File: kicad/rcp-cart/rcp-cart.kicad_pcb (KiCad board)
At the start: 2 copper layers, 2 parts

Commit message: WIP
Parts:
- CONN_EXP2: moved to B.Cu
- moved CONN_EXP2 11.8 mm to (207.3, 111.4), turned to 180 degrees

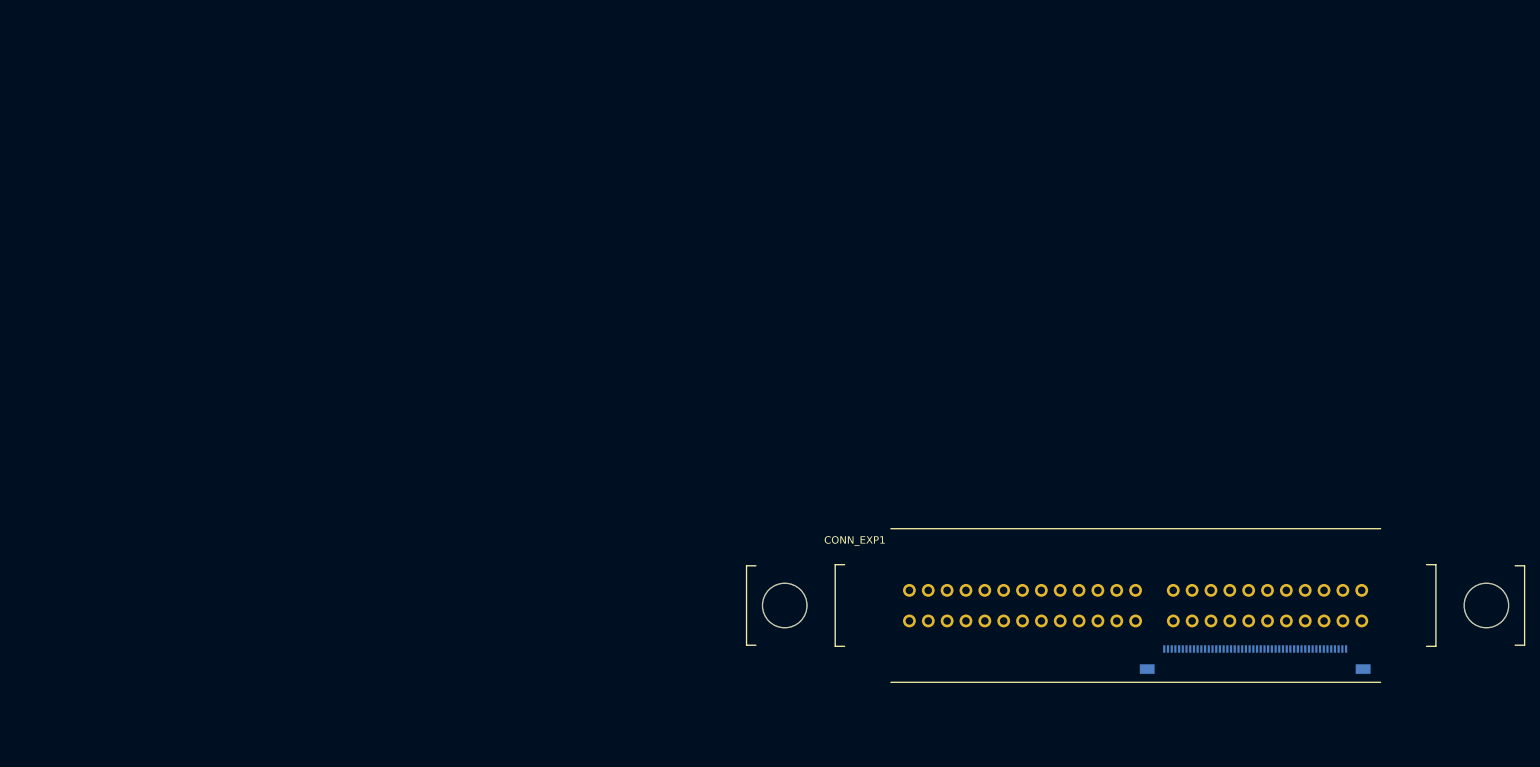
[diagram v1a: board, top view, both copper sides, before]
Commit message: Routing in progress, almost completed
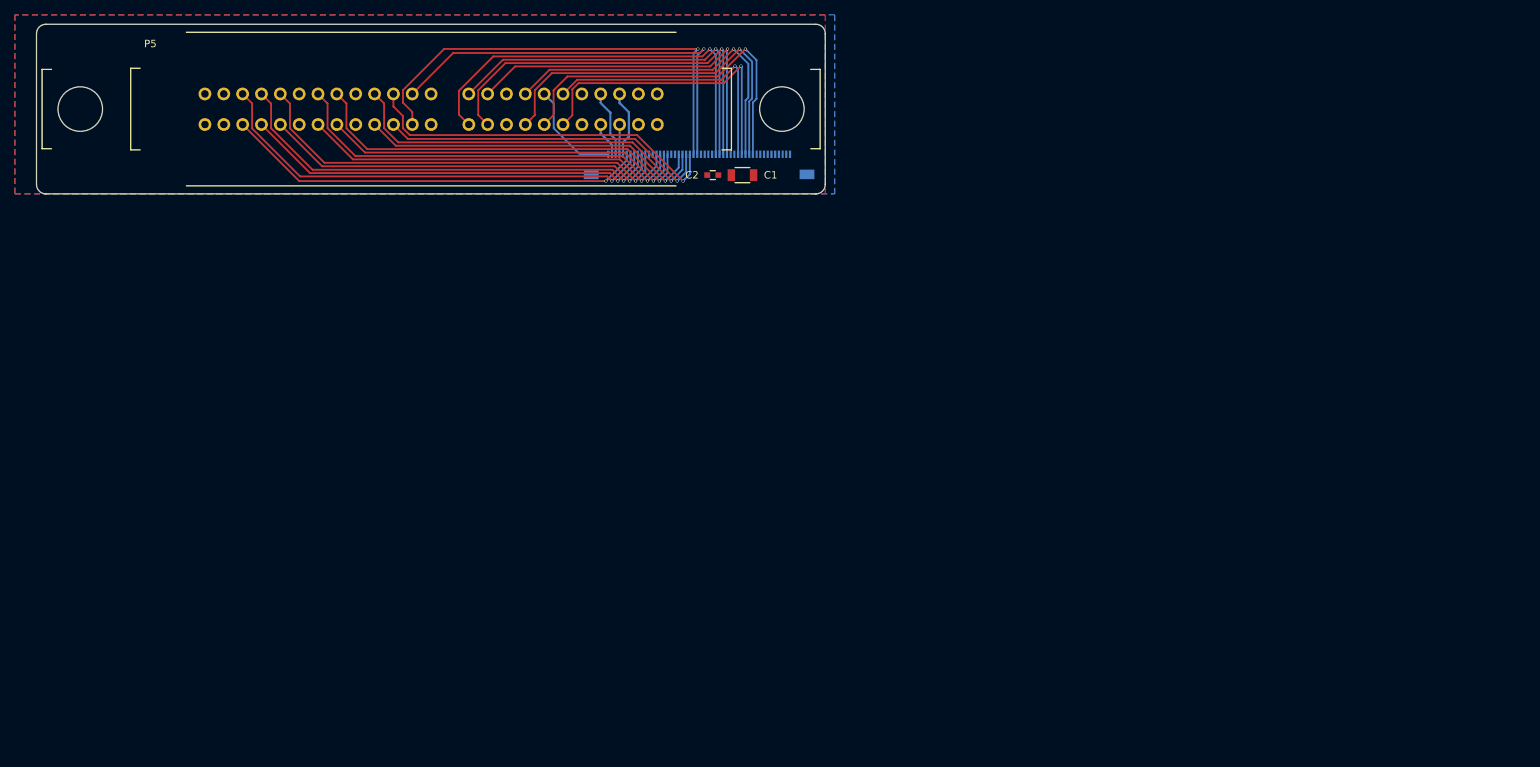
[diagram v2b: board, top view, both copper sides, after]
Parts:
- removed CONN_EXP1: CART-EDGE, n64:cart-edge-2x25-2.54mm
- removed CONN_EXP2: CART-EDGE, n64:connector-molex-502790-5091
- added C1: 4.7uF, n64:C_1206, F.Cu at (126.0, 47.0)
- added C2: .1uF, n64:C_0603, F.Cu at (122.0, 47.0)
- added P5: CART-EDGE, n64:cart-edge-2x25-2.54mm, F.Cu at (53.6, 38.1)
- added TO MAIN BOARD: 502790-5091, n64:connector-molex-502790-5091, B.Cu at (132.4, 44.7)
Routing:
- net /CART_ADDR10: track 0.00 -> 61.6 mm, vias 0 -> 1
- net /CART_ADDR00: track 0.00 -> 61.2 mm, vias 0 -> 1
- net /CART_ADDR01: track 0.00 -> 60.0 mm, vias 0 -> 1
- net /CART_ADDR02: track 0.00 -> 58.8 mm, vias 0 -> 1
- net /CART_ADDR15: track 0.00 -> 56.9 mm, vias 0 -> 1
- net /CART_ADDR05: track 0.00 -> 56.4 mm, vias 0 -> 1
- net /CART_ADDR09: track 0.00 -> 55.8 mm, vias 0 -> 1
- net /CART_ADDR14: track 0.00 -> 55.7 mm, vias 0 -> 1
- net /CART_ADDR03: track 0.00 -> 55.5 mm, vias 0 -> 1
- net /CART_ADDR08: track 0.00 -> 54.5 mm, vias 0 -> 1
- net /CART_ADDR13: track 0.00 -> 54.5 mm, vias 0 -> 1
- net /CART_ALE_L: track 0.00 -> 54.3 mm, vias 0 -> 1
- net /CART_ADDR12: track 0.00 -> 51.2 mm, vias 0 -> 1
- net /CART_ALE_H: track 0.00 -> 51.0 mm, vias 0 -> 1
- net /CART_ADDR06: track 0.00 -> 50.2 mm, vias 0 -> 1
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- added copper zone on B.Cu, net GND
- added copper zone on F.Cu, net GND
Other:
- board outline added: 106.3 x 22.9 mm
- net class Default: via_dia 0.6 -> 0.4; via_drill 0.4 -> 0.3
- net class PWR added: clearance 0.2, trace_width 0.3, via_dia 0.5, via_drill 0.3
- board text added: "1"
- board text added: "50"

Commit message: Almost done
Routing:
- net GND: track 27.2 -> 29.8 mm
- net /CART_ADDR10: track 61.6 -> 63.1 mm
- net /CART_ADDR08: track 54.5 -> 56.0 mm
- net /CART_ADDR07: track 49.1 -> 50.5 mm
- net /CART_ADDR09: track 55.8 -> 57.2 mm
- net /CART_ADDR06: track 50.2 -> 51.6 mm
- net /CART_ADDR05: track 56.4 -> 57.8 mm
- net /PIF_CIC_DAT_OUT: track 50.1 -> 51.2 mm
- net /PIF_CIC_DAT_IN: track 45.8 -> 46.8 mm
- net /CIC_CLK: track 48.3 -> 49.3 mm

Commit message: Completed, to do checks
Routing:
- net +3V3: track 0.00 -> 232.4 mm, vias 0 -> 29
- net GND: track 29.8 -> 93.1 mm, vias 0 -> 20
- net /EEPROM_DAT: track 0.00 -> 45.9 mm, vias 0 -> 1
- net //NMI: track 36.8 -> 38.2 mm
- net //COLDRESET: track 41.2 -> 42.6 mm

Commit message: Final version revision 1
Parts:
- added REF**: ViaStitch, n64:ViaStitch, F.Cu at (128.7, 35.4)
- added REF**: ViaStitch, n64:ViaStitch, F.Cu at (135.1, 38.1)
- added REF**: ViaStitch, n64:ViaStitch, F.Cu at (40.3, 36.6)
- added REF**: ViaStitch, n64:ViaStitch, F.Cu at (39.5, 35.4)
- added REF**: ViaStitch, n64:ViaStitch, F.Cu at (38.4, 34.7)
- added REF**: ViaStitch, n64:ViaStitch, F.Cu at (36.8, 34.3)
- added REF**: ViaStitch, n64:ViaStitch, F.Cu at (35.2, 34.7)
- added REF**: ViaStitch, n64:ViaStitch, F.Cu at (34.0, 35.4)
- added REF**: ViaStitch, n64:ViaStitch, F.Cu at (33.3, 36.6)
- added REF**: ViaStitch, n64:ViaStitch, F.Cu at (33.0, 38.1)
- added REF**: ViaStitch, n64:ViaStitch, F.Cu at (33.3, 39.5)
- added REF**: ViaStitch, n64:ViaStitch, F.Cu at (129.8, 34.7)
- added REF**: ViaStitch, n64:ViaStitch, F.Cu at (34.0, 40.8)
- added REF**: ViaStitch, n64:ViaStitch, F.Cu at (35.2, 41.5)
- added REF**: ViaStitch, n64:ViaStitch, F.Cu at (36.7, 41.9)
- added REF**: ViaStitch, n64:ViaStitch, F.Cu at (38.2, 41.7)
- added REF**: ViaStitch, n64:ViaStitch, F.Cu at (39.5, 40.8)
- added REF**: ViaStitch, n64:ViaStitch, F.Cu at (40.3, 39.6)
- added REF**: ViaStitch, n64:ViaStitch, F.Cu at (40.6, 38.1)
- added REF**: ViaStitch, n64:ViaStitch, F.Cu at (131.3, 34.3)
- added REF**: ViaStitch, n64:ViaStitch, F.Cu at (132.8, 34.7)
- added REF**: ViaStitch, n64:ViaStitch, F.Cu at (134.1, 35.6)
- added REF**: ViaStitch, n64:ViaStitch, F.Cu at (134.7, 36.6)
- added REF**: ViaStitch, n64:ViaStitch, F.Cu at (132.8, 41.7)
- added REF**: ViaStitch, n64:ViaStitch, F.Cu at (134.1, 40.8)
- added REF**: ViaStitch, n64:ViaStitch, F.Cu at (134.9, 39.6)
- added REF***: WEEE-Logo_4.2x6mm_SilkScreen, n64:WEEE-Logo_4.2x6mm_SilkScreen, F.Cu at (48.3, 37.7)
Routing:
- net +3V3: track 232.4 -> 223.7 mm
- net GND: track 93.1 -> 89.0 mm
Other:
- board text added: "Designed by dmkfasi"
- board text added: "Top side"

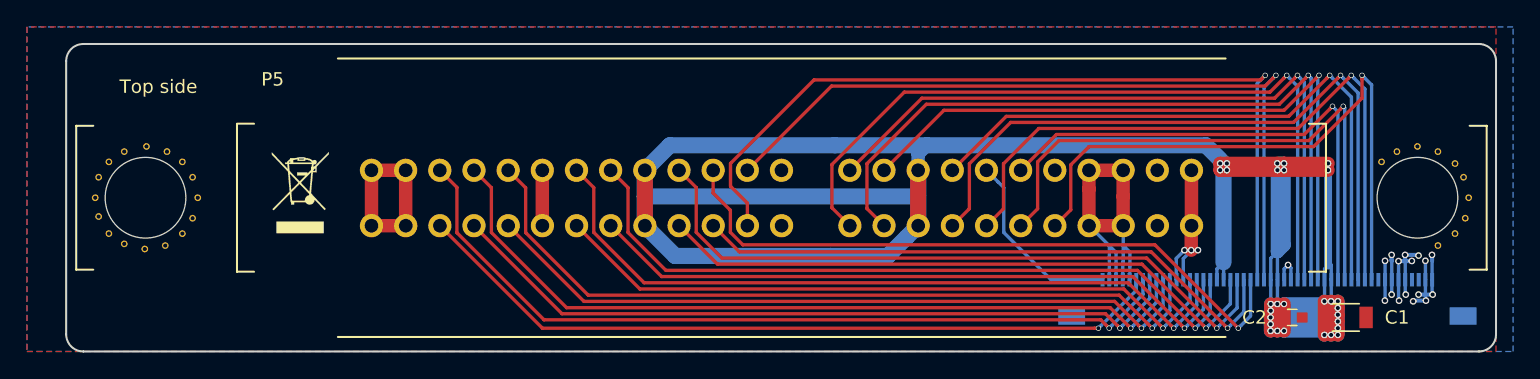
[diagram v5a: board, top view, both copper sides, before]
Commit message: Fixing in progress for new CART EDGE footprint
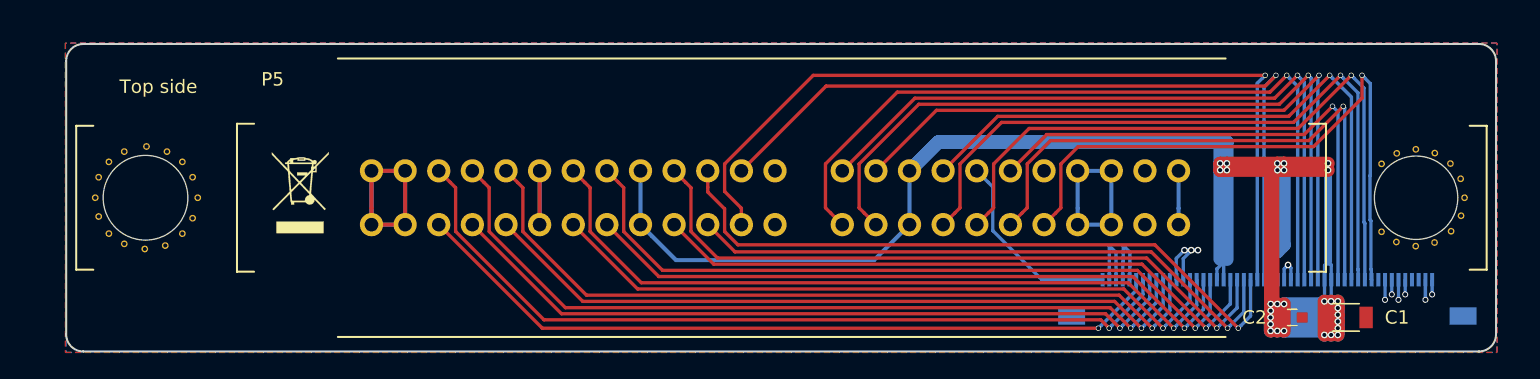
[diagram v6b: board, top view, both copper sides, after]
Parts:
- added REF**: ViaStitch, n64:ViaStitch, F.Cu at (128.7, 40.6)
- added REF**: ViaStitch, n64:ViaStitch, F.Cu at (129.8, 41.4)
- added REF**: ViaStitch, n64:ViaStitch, F.Cu at (131.2, 41.7)
- moved REF** 0.36 mm to (134.6, 39.4)
- moved REF** 0.34 mm to (133.8, 35.6)
- moved REF** 0.34 mm to (133.8, 40.6)
- moved REF** 0.34 mm to (132.6, 41.4)
- moved REF** 0.31 mm to (134.8, 38.1)
- moved REF** 0.26 mm to (132.6, 34.8)
- moved REF** 0.25 mm to (134.5, 36.7)
- moved REF** 0.24 mm to (131.2, 34.5)
- moved REF** 0.15 mm to (128.7, 35.6)
- moved REF** 0.13 mm to (129.8, 34.8)
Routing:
- net GND: track 89.0 -> 77.7 mm, vias 20 -> 10
- net +3V3: track 223.7 -> 227.8 mm
- net //NMI: track 38.2 -> 39.0 mm
- net /EEPROM_DAT: track 45.9 -> 46.7 mm
- net /PIF_CIC_DAT_IN: track 46.8 -> 47.5 mm
- net /JTCK: track 14.0 -> 14.6 mm
- net /CIC_CLK: track 49.3 -> 50.0 mm
- net /CART_ADDR07: track 50.5 -> 51.1 mm
- net /PIF_CIC_DAT_OUT: track 51.2 -> 51.8 mm
- net //COLDRESET: track 42.6 -> 43.2 mm
- net /CART_ADDR06: track 51.6 -> 52.2 mm
